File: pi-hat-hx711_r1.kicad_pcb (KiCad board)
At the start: 4 copper layers, 65 x 56 mm, 52 parts, among them J1 GPIO, J2 Conn_01x06, J3 Conn_01x06, J4 Conn_01x06, J5 Conn_01x06, Q1 S8550, U1 M24c64, U2 HX711, U3 TPS7A2050PDQNR, U4 TPS61040DBV

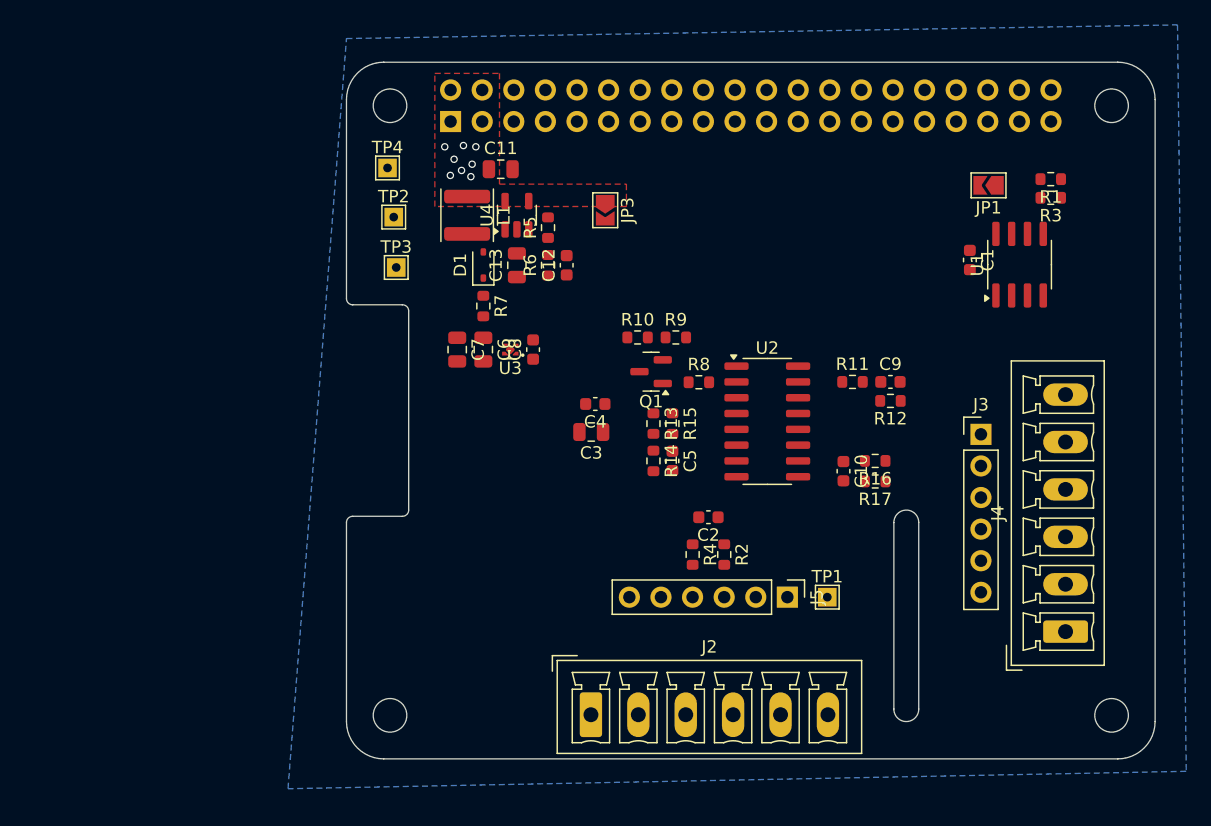
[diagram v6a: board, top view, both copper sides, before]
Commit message: chunk out routing
looks okish?

switched x2son for plain sot235, it's better stocked at jlc anyway, and
easier to probe and work with.
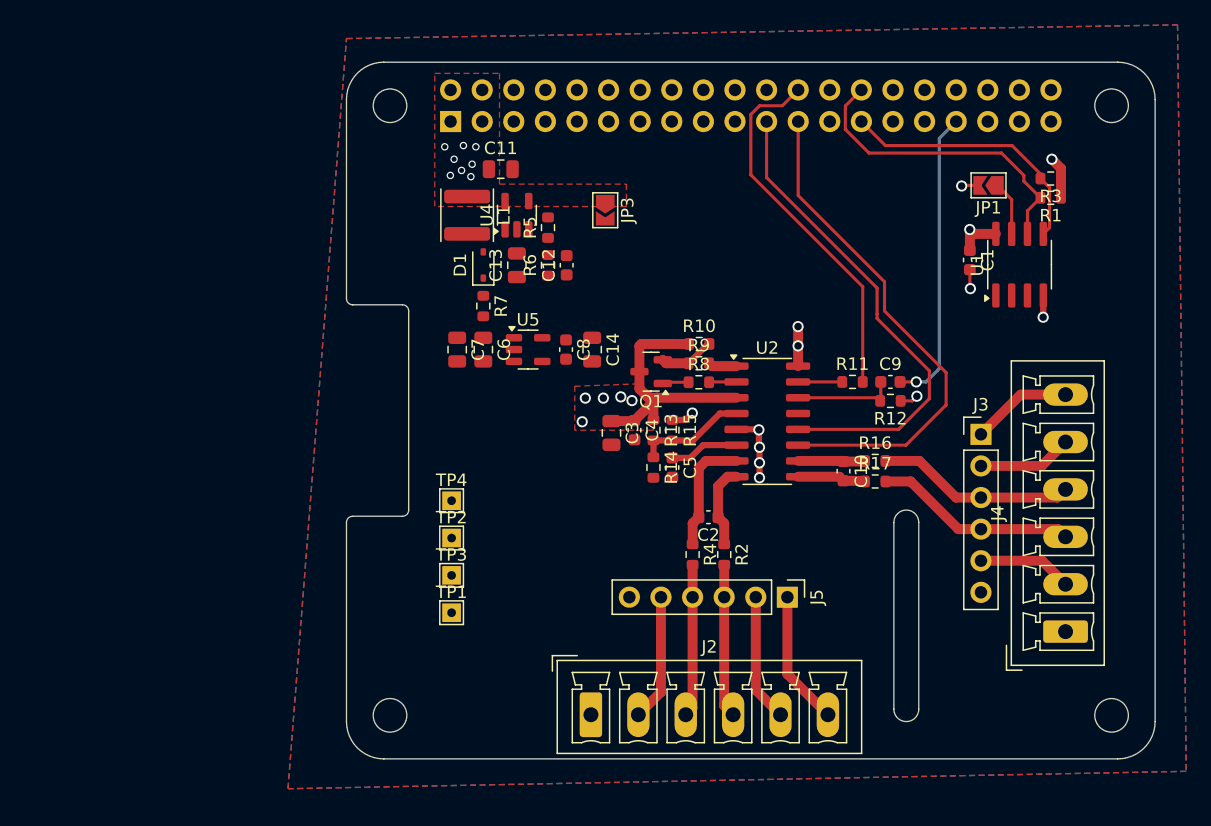
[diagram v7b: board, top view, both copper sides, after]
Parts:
- removed U3: TPS7A2050PDQNR, Package_SON:Texas_X2SON-4_1x1mm_P0.65mm
- added C14: 10uF, Capacitor_SMD:C_0805_2012Metric, F.Cu at (119.8, 67.1)
- added U5: TPS7A2050PDBV, Package_TO_SOT_SMD:SOT-23-5, F.Cu at (114.6, 67.1)
- moved TP1 30.2 mm to (108.5, 88.2)
- moved TP4 27.2 mm to (108.5, 79.2)
- moved TP2 26.2 mm to (108.5, 82.2)
- moved TP3 25.1 mm to (108.5, 85.2)
- moved R10 4.98 mm to (128.3, 66.7)
- moved C4 3.79 mm to (123.2, 73.6), turned to -90 degrees
- moved R9 2.78 mm to (128.3, 68.2)
- moved C8 2.65 mm to (117.7, 67.1), turned to -90 degrees
- moved C3 1.63 mm to (121.3, 73.8), turned to -90 degrees
- moved R3 1.55 mm to (156.6, 53.4)
- moved R1 1.50 mm to (156.6, 54.9)
- moved C5 0.53 mm to (126.2, 76.6)
- moved R13 0.53 mm to (124.7, 73.6)
- moved R14 0.53 mm to (124.7, 76.6)
- moved R15 0.53 mm to (126.2, 73.6)
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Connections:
- C10 pad 1: /BR_OUT2+ -> /Analog/INB+
- C10 pad 2: /BR_OUT2- -> /Analog/INB-
- R16 pad 1: /BR_OUT2+ -> /Analog/INB+
- R17 pad 1: /BR_OUT2- -> /Analog/INB-
- U2 pad 10: /BR_OUT2+ -> /Analog/INB+
- U2 pad 9: /BR_OUT2- -> /Analog/INB-
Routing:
- net /GPIO11/SPI0.SCLK: track 0.00 -> 40.9 mm
- net /EXE1+: track 0.00 -> 40.9 mm, vias 0 -> 5
- net /GPIO9/SPI0.MISO: track 0.00 -> 39.3 mm
- net /GPIO8/SPI0.CE0: track 0.00 -> 29.9 mm
- net /ID_SCL: track 0.00 -> 25.3 mm
- net /GPIO13/PWM1: track 0.00 -> 24.0 mm, vias 0 -> 1
- net /ID_SDA: track 0.00 -> 21.5 mm
- net /BR_OUT2-: track 0.00 -> 16.3 mm
- net /BR_OUT2+: track 0.00 -> 16.0 mm
- net /BR_OUT1+: track 0.00 -> 12.4 mm
- net /BR_OUT1-: track 0.00 -> 12.3 mm
- net GND: track 0.00 -> 12.3 mm, vias 0 -> 8
- net +3V3: track 0.00 -> 12.0 mm, vias 0 -> 5
- net /REFIN1+: track 0.00 -> 10.3 mm
- net /REFIN1-: track 0.00 -> 10.2 mm
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- added copper zone on F.Cu, net /EXE1+
- added copper zone on In2.Cu, net /EXE1+
- added copper zone on F.Cu, net GND

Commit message: pushing silk, are we done?!
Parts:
- moved JP3 7.12 mm to (122.0, 62.9)
- moved TP2 6.13 mm to (108.5, 88.4)
- moved TP1 3.13 mm to (108.5, 91.4)
- moved TP4 3.13 mm to (108.5, 82.4)
- moved TP3 0.15 mm to (108.5, 85.4)
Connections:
- net Net-(U5-EN) renamed /power/VBOOST_F
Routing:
- net /EXE1+: track 40.9 -> 110.0 mm
- net /power/VBOOST: track 0.00 -> 38.5 mm
- net VDDA: track 2.30 -> 27.2 mm, vias 0 -> 1
- net +5V: track 0.00 -> 20.2 mm, vias 8 -> 7
- net Net-(D1-A): track 0.00 -> 5.19 mm
- net Net-(U4-FB): track 0.00 -> 4.73 mm
- net /power/VBOOST_F: track 0.00 -> 3.86 mm
- net GND: vias 8 -> 23
- added copper zone on F.Cu, net /power/VBOOST_F
- added copper zone on F.Cu, net VDDA
- removed copper zone on In2.Cu, net VDDA
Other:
- board text added: "EXE+"
- board text added: "GND"
- board text added: "VBoost"
- board text added: "VDDA"
